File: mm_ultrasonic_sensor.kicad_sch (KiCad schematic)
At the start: 0 parts

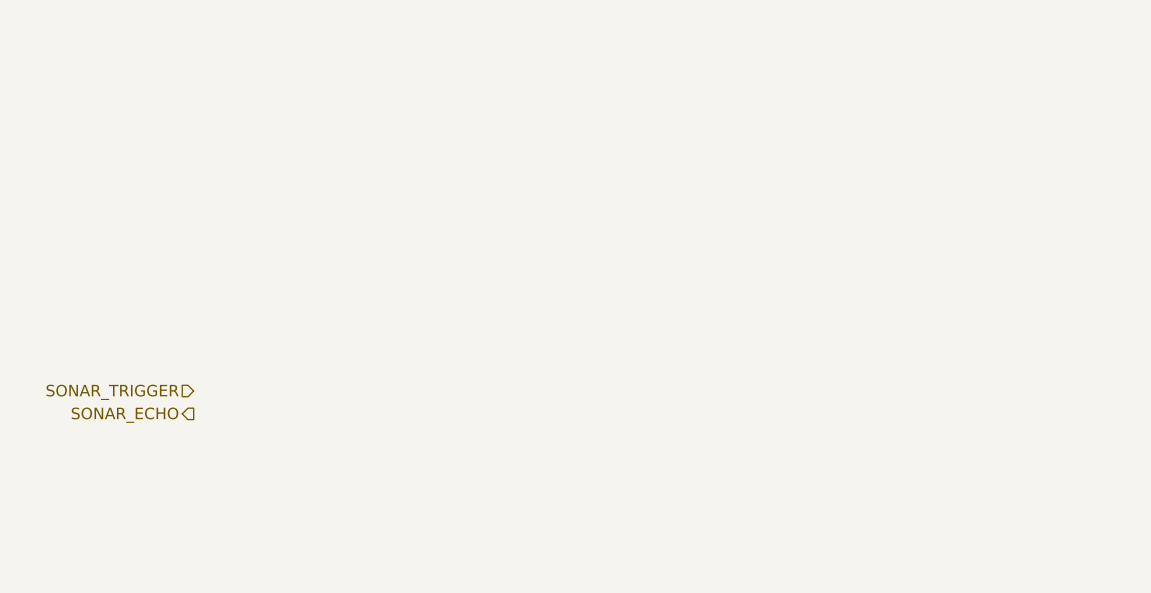
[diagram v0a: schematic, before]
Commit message: ended PCB + added reverse voltage protection
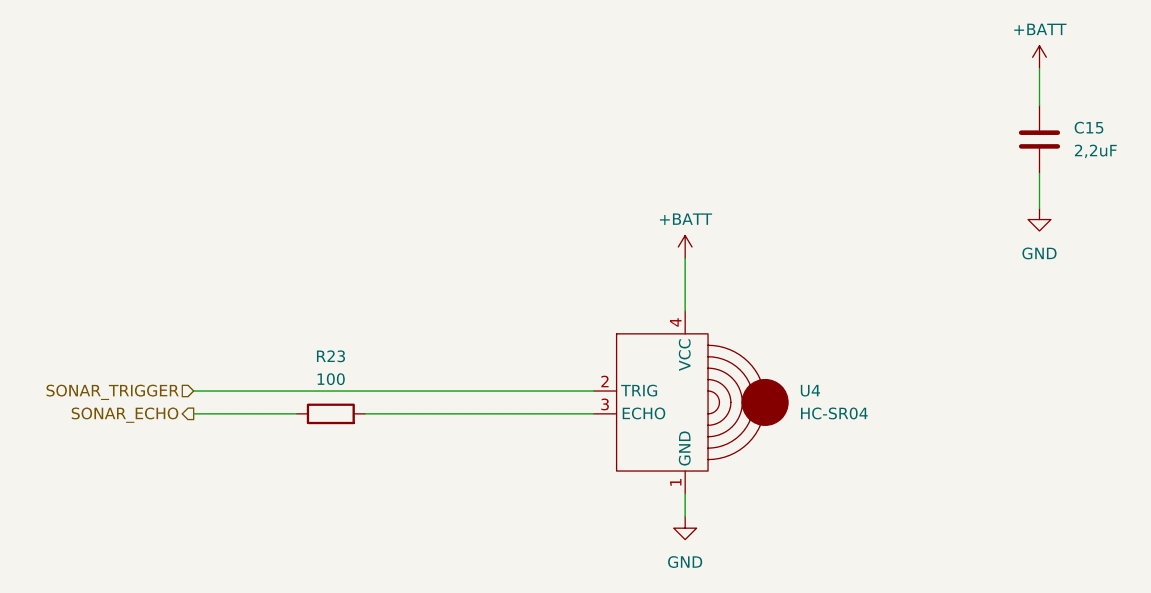
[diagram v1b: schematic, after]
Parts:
- added C15: 2,2uF, Capacitor_SMD:C_0603_1608Metric, symbol Device:C
- added R23: 100, Resistor_SMD:R_0603_1608Metric, symbol Device:R
- added U4: HC-SR04, minimouse:HC-SR04, symbol minimouse:HC-SR04
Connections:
- net SONAR_ECHO: now also R23.1
- net SONAR_TRIGGER: now also U4.2 (TRIG)
- new net: R23.2, U4.3 (ECHO)
- new net +BATT: C15.1, U4.4 (VCC)
- new net GND: C15.2, U4.1 (GND)
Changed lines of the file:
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@@
 (kicad_sch (version 20230121) (generator eeschema)
   (paper "A4")
+  (wire (pts (xy 163.83 100.33) (xy 163.83 102.87))
+    (stroke (width 0) (type default))
+  )
+  (wire (pts (xy 203.2 53.086) (xy 203.2 57.15))
+    (stroke (width 0) (type default))
+  )
+  (wire (pts (xy 109.22 91.44) (xy 120.65 91.44))
+    (stroke (width 0) (type default))
+  )
+  (wire (pts (xy 109.22 88.9) (xy 153.67 88.9))
+    (stroke (width 0) (type default))
+  )
+  (wire (pts (xy 128.27 91.44) (xy 153.67 91.44))
+    (stroke (width 0) (type default))
+  )
+  (wire (pts (xy 163.83 74.168) (xy 163.83 80.01))
+    (stroke (width 0) (type default))
+  )
+  (wire (pts (xy 203.2 64.77) (xy 203.2 68.58))
+    (stroke (width 0) (type default))
+  )
   (hierarchical_label "SONAR_TRIGGER" (shape input) (at 109.22 88.9 180) (fields_autoplaced)
     (effects (font (size 1.27 1.27)) (justify right))
@@
     (effects (font (size 1.27 1.27)) (justify right))
   )
+  (symbol (lib_id "Device:C") (at 203.2 60.96 0) (unit 1)
+    (in_bom yes) (on_board yes) (dnp no) (fields_autoplaced)
+    (property "Reference" "C15" (at 207.01 59.69 0)
+      (effects (font (size 1.27 1.27)) (justify left))
+    )
+    (property "Value" "2,2uF" (at 207.01 62.23 0)
+      (effects (font (size 1.27 1.27)) (justify left))
+    )
+    (property "Footprint" "Capacitor_SMD:C_0603_1608Metric" (at 204.1652 64.77 0)
+      (effects (font (size 1.27 1.27)) hide)
+    )
+    (property "Datasheet" "~" (at 203.2 60.96 0)
+      (effects (font (size 1.27 1.27)) hide)
+    )
+    (pin "1")
+    (pin "2")
+    (instances
+      (project "minimouse"
+        (path "/d8fa4cba-2469-4231-847f-065b6b829f44/224298a9-7d6e-4a70-a0a5-f2614895ec28"
+          (reference "C15") (unit 1)
+        )
+      )
+    )
+  )
+  (symbol (lib_id "Device:R") (at 124.46 91.44 90) (unit 1)
+    (in_bom yes) (on_board yes) (dnp no) (fields_autoplaced)
+    (property "Reference" "R23" (at 124.46 85.09 90)
+      (effects (font (size 1.27 1.27)))
+    )
+    (property "Value" "100" (at 124.46 87.63 90)
+      (effects (font (size 1.27 1.27)))
+    )
+    (property "Footprint" "Resistor_SMD:R_0603_1608Metric" (at 124.46 93.218 90)
+      (effects (font (size 1.27 1.27)) hide)
+    )
+    (property "Datasheet" "~" (at 124.46 91.44 0)
+      (effects (font (size 1.27 1.27)) hide)
+    )
+    (pin "1")
+    (pin "2")
+    (instances
+      (project "minimouse"
+        (path "/d8fa4cba-2469-4231-847f-065b6b829f44/224298a9-7d6e-4a70-a0a5-f2614895ec28"
+          (reference "R23") (unit 1)
+        )
+      )
+    )
+  )
+  (symbol (lib_id "power:+BATT") (at 203.2 53.086 0) (unit 1)
+    (in_bom yes) (on_board yes) (dnp no) (fields_autoplaced)
+    (property "Reference" "#PWR034" (at 203.2 56.896 0)
+      (effects (font (size 1.27 1.27)) hide)
+    )
+    (property "Value" "+BATT" (at 203.2 48.768 0)
+      (effects (font (size 1.27 1.27)))
+    )
+    (property "Footprint" "" (at 203.2 53.086 0)
+      (effects (font (size 1.27 1.27)) hide)
+    )
+    (property "Datasheet" "" (at 203.2 53.086 0)
+      (effects (font (size 1.27 1.27)) hide)
+    )
+    (pin "1")
+    (instances
+      (project "minimouse"
+        (path "/d8fa4cba-2469-4231-847f-065b6b829f44/224298a9-7d6e-4a70-a0a5-f2614895ec28"
+          (reference "#PWR034") (unit 1)
+        )
+      )
+    )
+  )
+  (symbol (lib_id "power:+BATT") (at 163.83 74.168 0) (unit 1)
+    (in_bom yes) (on_board yes) (dnp no) (fields_autoplaced)
+    (property "Reference" "#PWR033" (at 163.83 77.978 0)
+      (effects (font (size 1.27 1.27)) hide)
+    )
+    (property "Value" "+BATT" (at 163.83 69.85 0)
+      (effects (font (size 1.27 1.27)))
+    )
+    (property "Footprint" "" (at 163.83 74.168 0)
+      (effects (font (size 1.27 1.27)) hide)
+    )
+    (property "Datasheet" "" (at 163.83 74.168 0)
+      (effects (font (size 1.27 1.27)) hide)
+    )
+    (pin "1")
+    (instances
+      (project "minimouse"
+        (path "/d8fa4cba-2469-4231-847f-065b6b829f44/224298a9-7d6e-4a70-a0a5-f2614895ec28"
+          (reference "#PWR033") (unit 1)
+        )
+      )
+    )
+  )
+  (symbol (lib_id "power:GND") (at 163.83 102.87 0) (unit 1)
+    (in_bom yes) (on_board yes) (dnp no) (fields_autoplaced)
+    (property "Reference" "#PWR032" (at 163.83 109.22 0)
+      (effects (font (size 1.27 1.27)) hide)
+    )
+    (property "Value" "GND" (at 163.83 107.95 0)
+      (effects (font (size 1.27 1.27)))
+    )
+    (property "Footprint" "" (at 163.83 102.87 0)
+      (effects (font (size 1.27 1.27)) hide)
+    )
+    (property "Datasheet" "" (at 163.83 102.87 0)
+      (effects (font (size 1.27 1.27)) hide)
+    )
+    (pin "1")
+    (instances
+      (project "minimouse"
+        (path "/d8fa4cba-2469-4231-847f-065b6b829f44/224298a9-7d6e-4a70-a0a5-f2614895ec28"
+          (reference "#PWR032") (unit 1)
+        )
+      )
+    )
+  )
+  (symbol (lib_id "power:GND") (at 203.2 68.58 0) (unit 1)
+    (in_bom yes) (on_board yes) (dnp no) (fields_autoplaced)
+    (property "Reference" "#PWR035" (at 203.2 74.93 0)
+      (effects (font (size 1.27 1.27)) hide)
+    )
+    (property "Value" "GND" (at 203.2 73.66 0)
+      (effects (font (size 1.27 1.27)))
+    )
+    (property "Footprint" "" (at 203.2 68.58 0)
+      (effects (font (size 1.27 1.27)) hide)
+    )
+    (property "Datasheet" "" (at 203.2 68.58 0)
+      (effects (font (size 1.27 1.27)) hide)
+    )
+    (pin "1")
+    (instances
+      (project "minimouse"
+        (path "/d8fa4cba-2469-4231-847f-065b6b829f44/224298a9-7d6e-4a70-a0a5-f2614895ec28"
+          (reference "#PWR035") (unit 1)
+        )
+      )
+    )
+  )
+  (symbol (lib_id "minimouse:HC-SR04") (at 163.83 90.17 0) (unit 1)
+    (in_bom yes) (on_board yes) (dnp no) (fields_autoplaced)
+    (property "Reference" "U4" (at 176.53 88.9 0)
+      (effects (font (size 1.27 1.27)) (justify left))
+    )
+    (property "Value" "HC-SR04" (at 176.53 91.44 0)
+      (effects (font (size 1.27 1.27)) (justify left))
+    )
+    (property "Footprint" "minimouse:HC-SR04" (at 163.83 90.17 0)
+      (effects (font (size 1.27 1.27)) hide)
+    )
+    (property "Datasheet" "" (at 163.83 90.17 0)
+      (effects (font (size 1.27 1.27)) hide)
+    )
+    (pin "1")
+    (pin "2")
+    (pin "3")
+    (pin "4")
+    (instances
+      (project "minimouse"
+        (path "/d8fa4cba-2469-4231-847f-065b6b829f44/224298a9-7d6e-4a70-a0a5-f2614895ec28"
+          (reference "U4") (unit 1)
+        )
+      )
+    )
+  )
 )
